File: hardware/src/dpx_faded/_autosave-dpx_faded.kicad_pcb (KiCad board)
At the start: 4 copper layers, 96.5 x 132.7 mm, 75 parts, among them J1 motor.1, J2 motor.2, J3 motor.3, J4 motor.4, SW1 TS-1187A-B-A-B, SW2 TS-1187A-B-A-B, U1 CH224K, U12 NML0505SC, U5 TC118S, U6 TC118S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

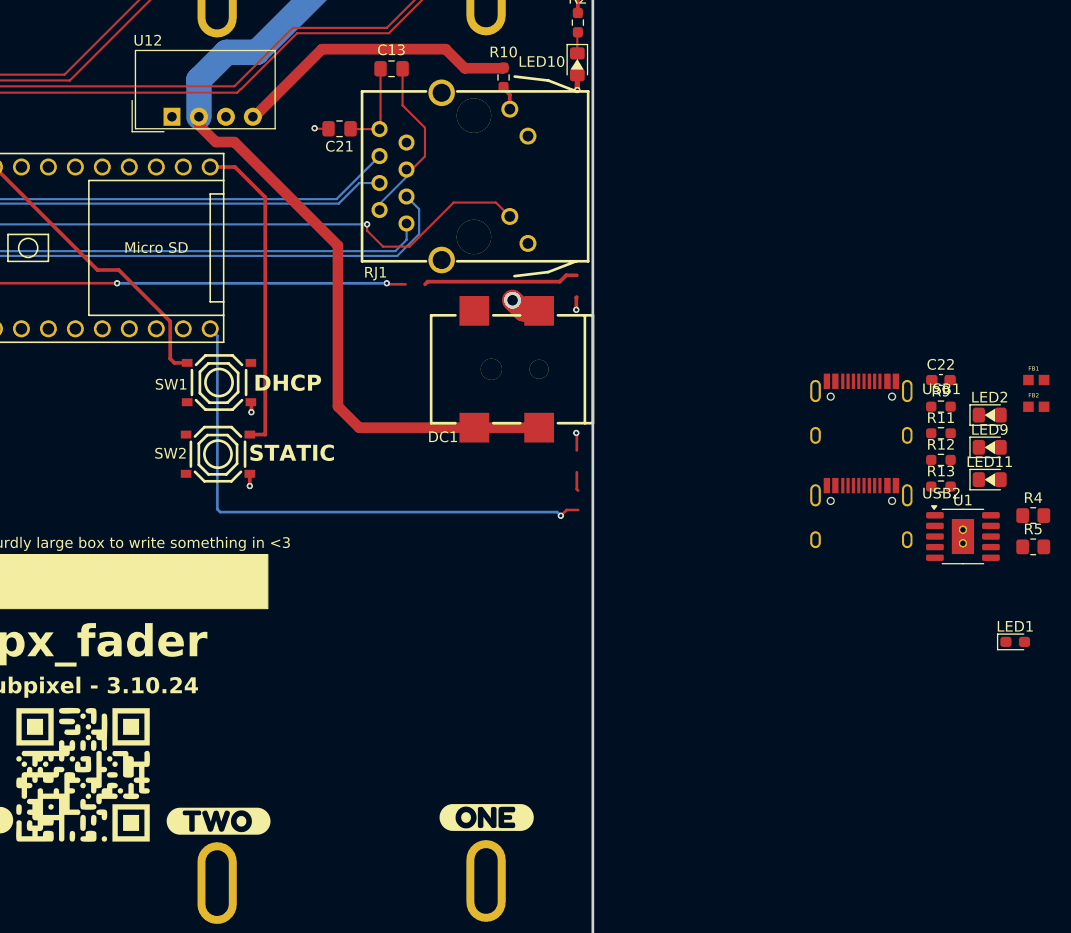
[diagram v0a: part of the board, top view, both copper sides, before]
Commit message: post v0.5.0 fixes--->(v0.6.0)
-----//HARDWARE
++ CH244 PD controller rough in
++ update PCB
++ add pdf for a fader

-----//FIRMWARE
++ add maxpatch to test faders
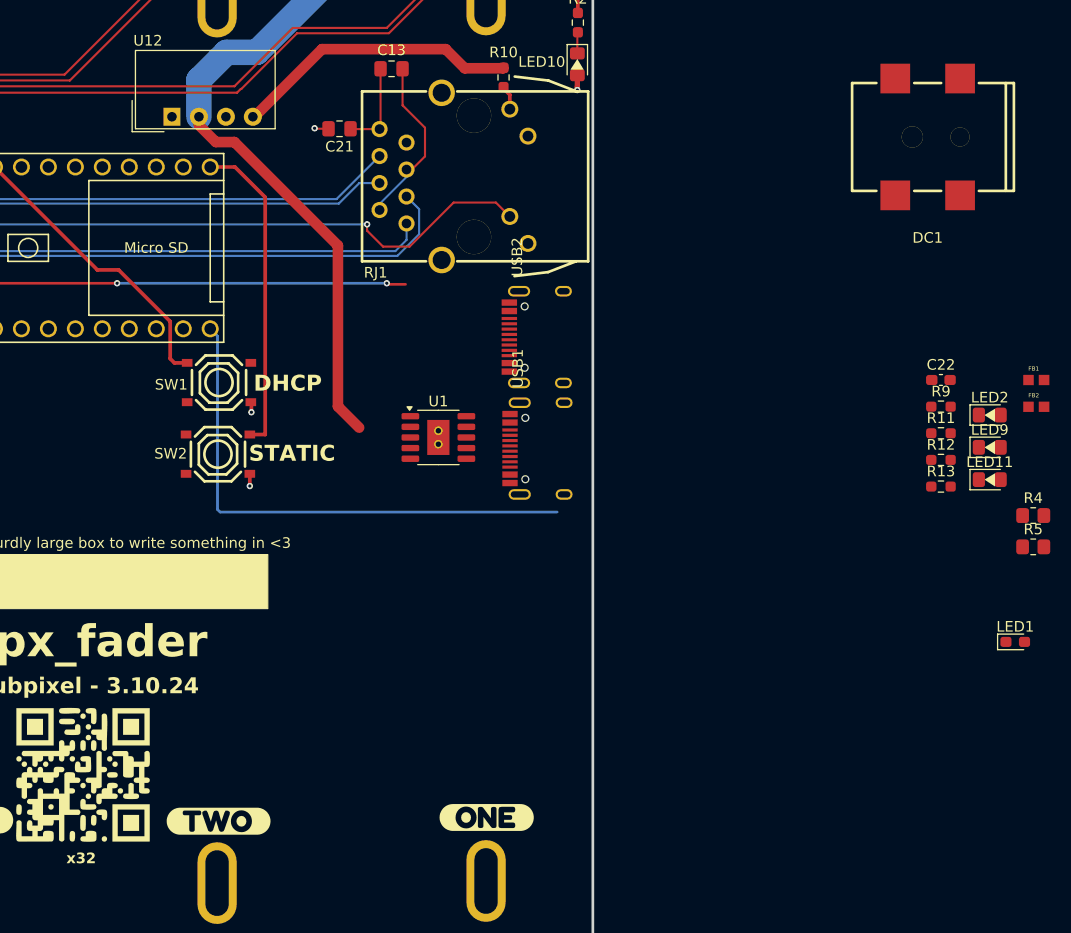
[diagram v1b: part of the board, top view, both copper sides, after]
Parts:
- moved U1 50.3 mm to (361.5, 172.2)
- moved DC1 45.3 mm to (407.6, 143.9)
- moved USB2 33.4 mm to (375.9, 162.8), turned to 90 degrees
- moved USB1 25.4 mm to (376.0, 173.3), turned to 90 degrees
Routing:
- net +5v-DIRTY: track 169.2 -> 152.2 mm
- net Net-(LED9-A): track 14.7 -> 0.00 mm
- net GND: track 43.0 -> 37.2 mm, vias 22 -> 19
- net LED6: track 51.8 -> 49.4 mm, vias 1 -> 0
- net Net-(LED11-A): track 1.78 -> 0.00 mm
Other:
- board text added: "x32"
